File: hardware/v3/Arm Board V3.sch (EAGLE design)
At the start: 48 parts, among them CN1 1X4-BIG, IC1 L6208D, IC2 L6208D, IC3 L6208D, Q3 Q_LTC490, U1 MAX3468CSA

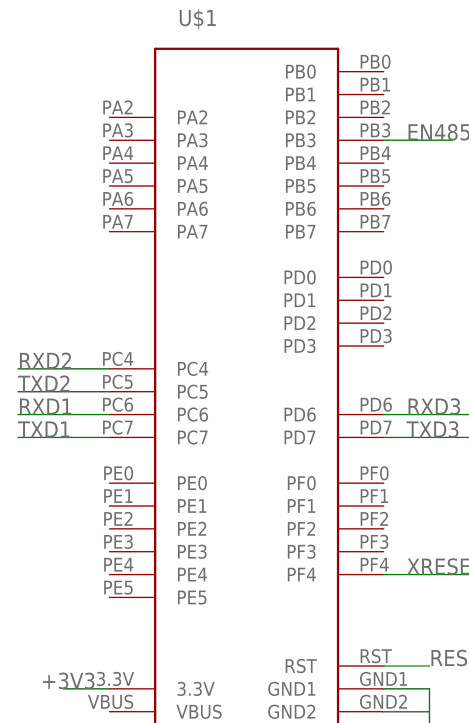
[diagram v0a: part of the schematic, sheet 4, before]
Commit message: Added enable pins to schematic and routed
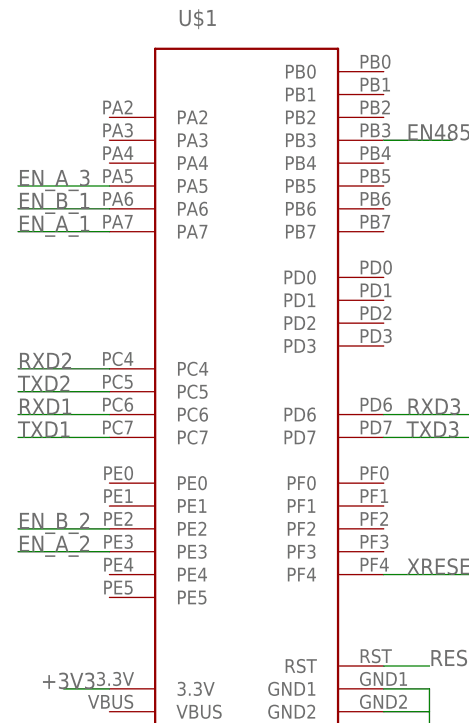
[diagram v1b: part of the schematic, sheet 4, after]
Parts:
- added H5: (no value), Lib_TH:H_MNTHOLE_#4
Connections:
- net EN_A_1: now also U$1.PA7
- net EN_A_2: now also U$1.PE3
- net EN_A_3: now also U$1.PA5
- net EN_B_1: now also U$1.PA6
- net EN_B_2: now also U$1.PE2
- net GND: now also H5.1
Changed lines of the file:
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@@
 <part name="GND13" library="SparkFun-Aesthetics" deviceset="GND" device=""/>
 <part name="GND14" library="SparkFun-Aesthetics" deviceset="GND" device=""/>
+<part name="H5" library="Lib_TH" deviceset="H_MNTHOLE" device="_#4"/>
+<part name="GND15" library="SparkFun-Aesthetics" deviceset="GND" device=""/>
 </parts>
 <sheets>
@@
 <instance part="GND13" gate="1" x="45.72" y="30.48"/>
 <instance part="GND14" gate="1" x="55.88" y="30.48"/>
+<instance part="H5" gate="G$1" x="66.04" y="38.1"/>
+<instance part="GND15" gate="1" x="66.04" y="30.48"/>
 </instances>
 <busses>
@@
 <pinref part="GND14" gate="1" pin="GND"/>
 <wire x1="55.88" y1="33.02" x2="55.88" y2="38.1" width="0.1524" layer="91"/>
+</segment>
+<segment>
+<pinref part="H5" gate="G$1" pin="1"/>
+<pinref part="GND15" gate="1" pin="GND"/>
+<wire x1="66.04" y1="33.02" x2="66.04" y2="38.1" width="0.1524" layer="91"/>
 </segment>
 </net>
@@
 </segment>
 </net>
+<net name="EN_A_1" class="0">
+<segment>
+<pinref part="U$1" gate="G$1" pin="PA7"/>
+<wire x1="12.7" y1="58.42" x2="2.54" y2="58.42" width="0.1524" layer="91"/>
+<label x="2.54" y="58.42" size="1.778" layer="95"/>
+</segment>
+</net>
+<net name="EN_A_3" class="0">
+<segment>
+<pinref part="U$1" gate="G$1" pin="PA5"/>
+<wire x1="12.7" y1="63.5" x2="2.54" y2="63.5" width="0.1524" layer="91"/>
+<label x="2.54" y="63.5" size="1.778" layer="95"/>
+</segment>
+</net>
+<net name="EN_A_2" class="0">
+<segment>
+<pinref part="U$1" gate="G$1" pin="PE3"/>
+<wire x1="12.7" y1="22.86" x2="2.54" y2="22.86" width="0.1524" layer="91"/>
+<label x="2.54" y="22.86" size="1.778" layer="95"/>
+</segment>
+</net>
+<net name="EN_B_2" class="0">
+<segment>
+<pinref part="U$1" gate="G$1" pin="PE2"/>
+<wire x1="12.7" y1="25.4" x2="2.54" y2="25.4" width="0.1524" layer="91"/>
+<label x="2.54" y="25.4" size="1.778" layer="95"/>
+</segment>
+</net>
+<net name="EN_B_1" class="0">
+<segment>
+<pinref part="U$1" gate="G$1" pin="PA6"/>
+<wire x1="12.7" y1="60.96" x2="2.54" y2="60.96" width="0.1524" layer="91"/>
+<label x="2.54" y="60.96" size="1.778" layer="95"/>
+</segment>
+</net>

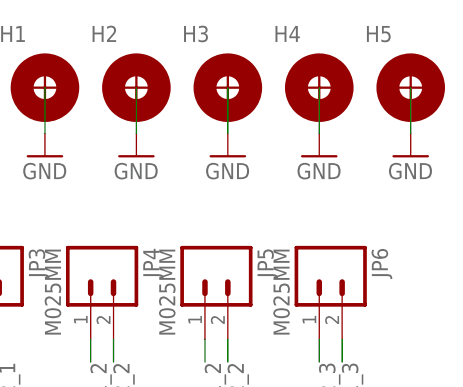
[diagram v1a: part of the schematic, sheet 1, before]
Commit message: Did some more routing on the board
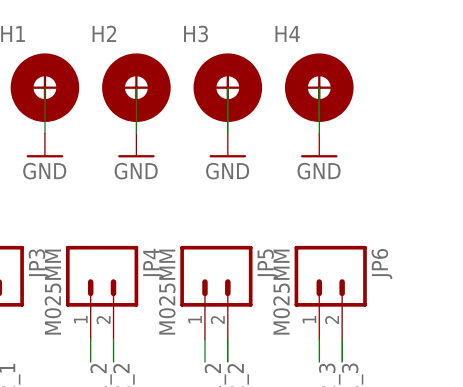
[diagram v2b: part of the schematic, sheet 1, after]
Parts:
- removed H5: (no value), Lib_TH:H_MNTHOLE_#4
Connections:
- removed net VS: C10.1, C3.1, C6.1, D2.A, D4.A, D6.A, IC1.VS_A, IC1.VS_B, IC2.VS_A, IC2.VS_B, IC3.VS_A, IC3.VS_B
- net GND: no longer H5.1
- net VIN: now also C10.1, C3.1, C6.1, D2.A, D4.A, D6.A, IC1.VS_A, IC1.VS_B, IC2.VS_A, IC2.VS_B, IC3.VS_A, IC3.VS_B

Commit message: Redid Xbee as well as moved things around
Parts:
- removed U$2: XBEE-1B2, SparkFun-RF:XBEE-1B2
- added C16: 0.1uF, SparkFun-Capacitors:0.1UF-25V(+80/-20%)(0603)
- added LED1, LED2: Red, SparkFun-LED:LED-RED0603
- added LED3, LED4, LED5: Green, SparkFun-LED:LED-GREEN0603
- added R12, R13, R14, R15, R16: 1k, SparkFun-Resistors:1KOHM1/10W1%(0603)
- added SJ2: SOLDERJUMPERTRACE, SparkFun:SOLDERJUMPERTRACE
- added U2: XBEE-1B3, SparkFun:XBEE-1B3
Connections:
- new net CTS: U2.CTS
- new net DIO0: U2.DIO0
- new net DIO1: U2.DIO1
- new net DIO11: U2.DIO11
- new net DIO12: U2.DIO12
- new net DIO2: U2.DIO2
- new net DIO3: SJ2.2, U2.DIO3
- new net DIO4: U2.DIO4
- new net DIO5: R16.2, U2.DIO5
- new net DIO9: U2.DIO9
- new net DTR: U2.DTR
- new net N$11: C16.2, SJ2.1
- new net N$139: LED5.A, R16.1
- new net N$38: LED1.A, R12.1
- new net N$4: LED2.A, R13.2
- new net N$6: LED3.A, R14.2
- new net N$7: LED4.A, R15.1
- new net RES1: U2.RES@8
- new net RES2: U2.RES@14
- new net RSSI: R15.2, U2.RSSI
- new net RTS: U2.RTS
- net +3V3: now also R12.2, R13.1, R14.1, U2.VDD; no longer U$2.VDD
- net GND: now also LED1.C, LED4.C, LED5.C, U2.GND; no longer U$2.GND
- net RXD3: now also LED2.C, U2.DOUT; no longer U$2.DOUT
- net TXD3: now also LED3.C, U2.DIN; no longer U$2.DIN
- net XRESET: now also C16.1, U2.RESET; no longer U$2.RESET

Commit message: Changed some stuff on launchpad
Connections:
- new net +5V: U$1.VBUS
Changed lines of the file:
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@@
 <part name="R15" library="SparkFun-Resistors" deviceset="1KOHM1/10W1%(0603)" device="" value="1k"/>
 <part name="GND17" library="SparkFun" deviceset="GND" device=""/>
-<part name="P+2" library="SparkFun" deviceset="3.3V" device=""/>
-<part name="P+3" library="SparkFun" deviceset="3.3V" device=""/>
-<part name="+3V3" library="SparkFun" deviceset="3.3V" device=""/>
 <part name="SJ2" library="SparkFun" deviceset="SOLDERJUMPER" device="TRACE"/>
 <part name="C16" library="SparkFun-Capacitors" deviceset="0.1UF-25V(+80/-20%)(0603)" device="" value="0.1uF"/>
@@
 </segment>
 </net>
+<net name="+5V" class="0">
+<segment>
+<pinref part="U$1" gate="G$1" pin="VBUS"/>
+<wire x1="12.7" y1="5.08" x2="7.62" y2="5.08" width="0.1524" layer="91"/>
+<label x="5.08" y="5.08" size="1.778" layer="95"/>
+</segment>
+</net>
 </nets>
 </sheet>
@@
 <instance part="R15" gate="G$1" x="17.78" y="81.28" rot="R90"/>
 <instance part="GND17" gate="1" x="17.78" y="60.96"/>
-<instance part="P+2" gate="G$1" x="30.48" y="88.9"/>
-<instance part="P+3" gate="G$1" x="5.08" y="88.9"/>
-<instance part="+3V3" gate="G$1" x="-5.08" y="88.9"/>
 <instance part="SJ2" gate="1" x="68.58" y="45.72"/>
 <instance part="C16" gate="G$1" x="50.8" y="45.72" rot="R90"/>
@@
 <wire x1="-5.08" y1="66.04" x2="-5.08" y2="63.5" width="0.1524" layer="91"/>
 <pinref part="LED2" gate="G$1" pin="C"/>
-<label x="-5.08" y="63.5" size="1.27" layer="95" rot="R270" xref="yes"/>
+<label x="-5.08" y="63.5" size="1.778" layer="95"/>
 </segment>
 <segment>
@@
 <wire x1="45.72" y1="86.36" x2="45.72" y2="88.9" width="0.1524" layer="91"/>
 <pinref part="R16" gate="G$1" pin="2"/>
-<label x="45.72" y="88.9" size="1.27" layer="95" rot="R90" xref="yes"/>
+<label x="45.72" y="88.9" size="1.778" layer="95"/>
 </segment>
 </net>
@@
 <wire x1="73.66" y1="45.72" x2="81.28" y2="45.72" width="0.1524" layer="91"/>
 <pinref part="SJ2" gate="1" pin="2"/>
-<label x="81.28" y="45.72" size="1.27" layer="95" xref="yes"/>
+<label x="81.28" y="45.72" size="1.778" layer="95"/>
 </segment>
 </net>
@@
 <wire x1="17.78" y1="86.36" x2="17.78" y2="88.9" width="0.1524" layer="91"/>
 <pinref part="R15" gate="G$1" pin="2"/>
-<label x="17.78" y="88.9" size="1.27" layer="95" rot="R90" xref="yes"/>
+<label x="17.78" y="88.9" size="1.778" layer="95"/>
 </segment>
 </net>
@@
 <wire x1="-5.08" y1="86.36" x2="-5.08" y2="88.9" width="0.1524" layer="91"/>
 <pinref part="R13" gate="G$1" pin="1"/>
-<pinref part="+3V3" gate="G$1" pin="3.3V"/>
+<label x="-5.08" y="88.9" size="1.778" layer="95"/>
 </segment>
 <segment>
 <wire x1="30.48" y1="88.9" x2="30.48" y2="86.36" width="0.1524" layer="91"/>
 <pinref part="R12" gate="G$1" pin="2"/>
-<pinref part="P+2" gate="G$1" pin="3.3V"/>
+<label x="30.48" y="88.9" size="1.778" layer="95"/>
 </segment>
 <segment>
 <wire x1="5.08" y1="86.36" x2="5.08" y2="88.9" width="0.1524" layer="91"/>
 <pinref part="R14" gate="G$1" pin="1"/>
-<pinref part="P+3" gate="G$1" pin="3.3V"/>
+<label x="5.08" y="88.9" size="1.778" layer="95"/>
 </segment>
 </net>
@@
 <wire x1="5.08" y1="66.04" x2="5.08" y2="63.5" width="0.1524" layer="91"/>
 <pinref part="LED3" gate="G$1" pin="C"/>
-<label x="5.08" y="63.5" size="1.27" layer="95" rot="R270" xref="yes"/>
+<label x="5.08" y="63.5" size="1.778" layer="95"/>
 </segment>
 </net>
@@
 <wire x1="45.72" y1="45.72" x2="35.56" y2="45.72" width="0.1524" layer="91"/>
 <pinref part="C16" gate="G$1" pin="1"/>
-<label x="35.56" y="45.72" size="1.27" layer="95" rot="R180" xref="yes"/>
-</segment>
-</net>
+<label x="35.56" y="45.72" size="1.778" layer="95"/>
+</segment>
+</net>

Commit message: Routed stuffs and stuffs and moved stuff and stuffs
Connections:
- net EN_A_1: now also U$1.PE1; no longer U$1.PA7
- net EN_A_2: now also U$1.PB7; no longer U$1.PE3
- net EN_A_3: no longer U$1.PA5
- net EN_B_1: now also U$1.PE2; no longer U$1.PA6
- net EN_B_2: now also U$1.PB6; no longer U$1.PE2
- net IN1_A_1: now also U$1.PD1
- net IN1_A_2: now also U$1.PA4
- net IN1_B_1: now also U$1.PD2
- net IN1_B_2: now also U$1.PA2
- net IN2_A_1: now also U$1.PD0
- net IN2_A_2: now also U$1.PA3
- net IN2_B_1: now also U$1.PD3
- net IN2_B_2: now also U$1.PE0
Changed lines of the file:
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@@
-</segment>
-</net>
-<net name="EN_A_1" class="0">
-<segment>
-<pinref part="U$1" gate="G$1" pin="PA7"/>
-<wire x1="12.7" y1="58.42" x2="2.54" y2="58.42" width="0.1524" layer="91"/>
-<label x="2.54" y="58.42" size="1.778" layer="95"/>
-</segment>
-</net>
-<net name="EN_A_3" class="0">
-<segment>
-<pinref part="U$1" gate="G$1" pin="PA5"/>
-<wire x1="12.7" y1="63.5" x2="2.54" y2="63.5" width="0.1524" layer="91"/>
-<label x="2.54" y="63.5" size="1.778" layer="95"/>
-</segment>
-</net>
-<net name="EN_A_2" class="0">
-<segment>
-<pinref part="U$1" gate="G$1" pin="PE3"/>
-<wire x1="12.7" y1="22.86" x2="2.54" y2="22.86" width="0.1524" layer="91"/>
-<label x="2.54" y="22.86" size="1.778" layer="95"/>
-</segment>
-</net>
-<net name="EN_B_2" class="0">
-<segment>
-<pinref part="U$1" gate="G$1" pin="PE2"/>
-<wire x1="12.7" y1="25.4" x2="2.54" y2="25.4" width="0.1524" layer="91"/>
-<label x="2.54" y="25.4" size="1.778" layer="95"/>
-</segment>
-</net>
-<net name="EN_B_1" class="0">
-<segment>
-<pinref part="U$1" gate="G$1" pin="PA6"/>
-<wire x1="12.7" y1="60.96" x2="2.54" y2="60.96" width="0.1524" layer="91"/>
-<label x="2.54" y="60.96" size="1.778" layer="95"/>
 </segment>
 </net>
@@
 </segment>
 </net>
+<net name="IN2_A_1" class="0">
+<segment>
+<pinref part="U$1" gate="G$1" pin="PD0"/>
+<wire x1="43.18" y1="53.34" x2="50.8" y2="53.34" width="0.1524" layer="91"/>
+<label x="45.72" y="53.34" size="1.778" layer="95"/>
+</segment>
+</net>
+<net name="IN1_B_1" class="0">
+<segment>
+<pinref part="U$1" gate="G$1" pin="PD2"/>
+<wire x1="43.18" y1="48.26" x2="50.8" y2="48.26" width="0.1524" layer="91"/>
+<label x="45.72" y="48.26" size="1.778" layer="95"/>
+</segment>
+</net>
+<net name="IN2_B_1" class="0">
+<segment>
+<pinref part="U$1" gate="G$1" pin="PD3"/>
+<wire x1="43.18" y1="45.72" x2="50.8" y2="45.72" width="0.1524" layer="91"/>
+<label x="45.72" y="45.72" size="1.778" layer="95"/>
+</segment>
+</net>
+<net name="EN_A_1" class="0">
+<segment>
+<pinref part="U$1" gate="G$1" pin="PE1"/>
+<wire x1="12.7" y1="27.94" x2="2.54" y2="27.94" width="0.1524" layer="91"/>
+<label x="2.54" y="27.94" size="1.778" layer="95"/>
+</segment>
+</net>
+<net name="EN_B_1" class="0">
+<segment>
+<pinref part="U$1" gate="G$1" pin="PE2"/>
+<wire x1="12.7" y1="25.4" x2="2.54" y2="25.4" width="0.1524" layer="91"/>
+<label x="2.54" y="25.4" size="1.778" layer="95"/>
+</segment>
+</net>
+<net name="IN1_A_1" class="0">
+<segment>
+<pinref part="U$1" gate="G$1" pin="PD1"/>
+<wire x1="43.18" y1="50.8" x2="50.8" y2="50.8" width="0.1524" layer="91"/>
+<label x="45.72" y="50.8" size="1.778" layer="95"/>
+</segment>
+</net>
+<net name="IN1_B_2" class="0">
+<segment>
+<pinref part="U$1" gate="G$1" pin="PA2"/>
+<wire x1="12.7" y1="71.12" x2="2.54" y2="71.12" width="0.1524" layer="91"/>
+<label x="2.54" y="71.12" size="1.778" layer="95"/>
+</segment>
+</net>
+<net name="IN2_A_2" class="0">
+<segment>
+<pinref part="U$1" gate="G$1" pin="PA3"/>
+<wire x1="12.7" y1="68.58" x2="2.54" y2="68.58" width="0.1524" layer="91"/>
+<label x="2.54" y="68.58" size="1.778" layer="95"/>
+</segment>
+</net>
+<net name="IN1_A_2" class="0">
+<segment>
+<pinref part="U$1" gate="G$1" pin="PA4"/>
+<wire x1="12.7" y1="66.04" x2="2.54" y2="66.04" width="0.1524" layer="91"/>
+<label x="2.54" y="66.04" size="1.778" layer="95"/>
+</segment>
+</net>
+<net name="EN_B_2" class="0">
+<segment>
+<pinref part="U$1" gate="G$1" pin="PB6"/>
+<wire x1="43.18" y1="60.96" x2="50.8" y2="60.96" width="0.1524" layer="91"/>
+<label x="45.72" y="60.96" size="1.778" layer="95"/>
+</segment>
+</net>
+<net name="EN_A_2" class="0">
+<segment>
+<pinref part="U$1" gate="G$1" pin="PB7"/>
+<wire x1="43.18" y1="58.42" x2="50.8" y2="58.42" width="0.1524" layer="91"/>
+<label x="45.72" y="58.42" size="1.778" layer="95"/>
+</segment>
+</net>
+<net name="IN2_B_2" class="0">
+<segment>
+<pinref part="U$1" gate="G$1" pin="PE0"/>
+<wire x1="12.7" y1="30.48" x2="2.54" y2="30.48" width="0.1524" layer="91"/>
+<label x="2.54" y="30.48" size="1.778" layer="95"/>
+</segment>
+</net>

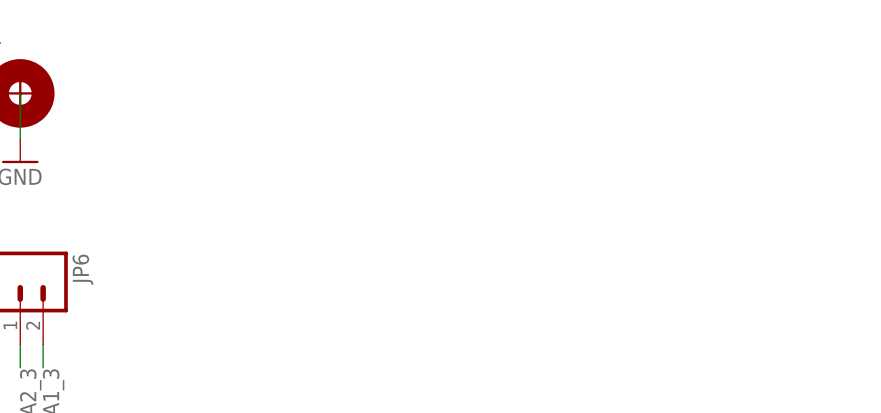
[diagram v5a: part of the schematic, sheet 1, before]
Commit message: Routing and Voltage Regulators (See Notes)
Started to route all of the pins towards the processor.  They need to be
reordered/reassigned since they do not make routing sense.  Added the
+12V and +18V regulators and hooked them up.  The +3V3 and +5V still
need to be picked and placed.
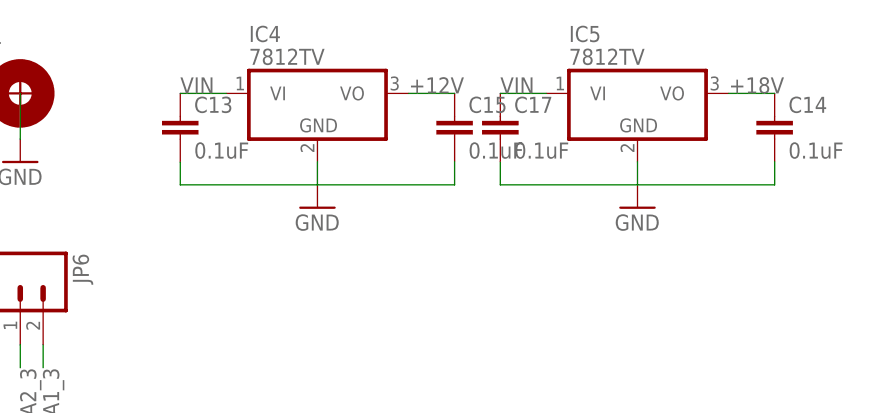
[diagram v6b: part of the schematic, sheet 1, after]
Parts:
- added C13, C14, C15, C17: 0.1uF, SparkFun-Capacitors:0.1UF-25V(+80/-20%)(0603)
- added IC4, IC5: 7812TV, linear:7812TV
- U1: value MAX3468CSA -> MAX3468CPA; device maxim:MAX3468CSA -> maxim:MAX3468CPA
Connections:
- new net +12V: C15.1, C3.1, D2.A, IC3.VS_A, IC3.VS_B, IC4.VO
- net +18V: now also C14.1, IC5.VO
- net EN_A_3: now also U$1.PB0
- net GND: now also C13.2, C14.2, C15.2, C17.2, IC4.GND, IC5.GND
- net IN1_A_3: now also U$1.PB1
- net IN2_A_3: now also U$1.PB2
- net VIN: now also C13.1, C17.1, IC4.VI, IC5.VI; no longer C3.1, D2.A, IC3.VS_A, IC3.VS_B
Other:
- note added: "TEMP!!! REPLACE!!!"
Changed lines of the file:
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@@
 <part name="IC2" library="L6206D" deviceset="L6208" device="D"/>
 <part name="IC3" library="L6206D" deviceset="L6208" device="D"/>
-<part name="U1" library="maxim" deviceset="MAX34*" device="SA" technology="68C" value="MAX3468CSA"/>
+<part name="U1" library="maxim" deviceset="MAX34*" device="PA" technology="68C" value="MAX3468CPA"/>
 <part name="CN1" library="adafruit" deviceset="1X4" device="-BIG"/>
 <part name="JP1" library="SparkFun-Connectors" deviceset="M02" device="5MM"/>
@@
 <part name="R16" library="SparkFun-Resistors" deviceset="1KOHM1/10W1%(0603)" device="" value="1k"/>
 <part name="GND31" library="SparkFun" deviceset="GND" device=""/>
+<part name="IC4" library="linear" deviceset="78*" device="TV" technology="12" value="7812TV"/>
+<part name="GND15" library="SparkFun-Aesthetics" deviceset="GND" device=""/>
+<part name="IC5" library="linear" deviceset="78*" device="TV" technology="12" value="7812TV"/>
+<part name="GND16" library="SparkFun-Aesthetics" deviceset="GND" device=""/>
+<part name="C13" library="SparkFun-Capacitors" deviceset="0.1UF-25V(+80/-20%)(0603)" device="" value="0.1uF"/>
+<part name="C14" library="SparkFun-Capacitors" deviceset="0.1UF-25V(+80/-20%)(0603)" device="" value="0.1uF"/>
+<part name="C15" library="SparkFun-Capacitors" deviceset="0.1UF-25V(+80/-20%)(0603)" device="" value="0.1uF"/>
+<part name="C17" library="SparkFun-Capacitors" deviceset="0.1UF-25V(+80/-20%)(0603)" device="" value="0.1uF"/>
 </parts>
 <sheets>
@@
 <instance part="GND13" gate="1" x="45.72" y="30.48"/>
 <instance part="GND14" gate="1" x="55.88" y="30.48"/>
+<instance part="IC4" gate="A1" x="88.9" y="38.1"/>
+<instance part="GND15" gate="1" x="88.9" y="25.4"/>
+<instance part="IC5" gate="A1" x="124.46" y="38.1"/>
+<instance part="GND16" gate="1" x="124.46" y="25.4"/>
+<instance part="C13" gate="G$1" x="73.66" y="33.02"/>
+<instance part="C14" gate="G$1" x="139.7" y="33.02"/>
+<instance part="C15" gate="G$1" x="104.14" y="33.02"/>
+<instance part="C17" gate="G$1" x="109.22" y="33.02"/>
 </instances>
 <busses>
@@
 <wire x1="55.88" y1="33.02" x2="55.88" y2="38.1" width="0.1524" layer="91"/>
 </segment>
+<segment>
+<pinref part="IC4" gate="A1" pin="GND"/>
+<wire x1="88.9" y1="30.48" x2="88.9" y2="27.94" width="0.1524" layer="91"/>
+<pinref part="GND15" gate="1" pin="GND"/>
+<wire x1="88.9" y1="27.94" x2="73.66" y2="27.94" width="0.1524" layer="91"/>
+<wire x1="73.66" y1="27.94" x2="73.66" y2="30.48" width="0.1524" layer="91"/>
+<wire x1="88.9" y1="27.94" x2="104.14" y2="27.94" width="0.1524" layer="91"/>
+<wire x1="104.14" y1="27.94" x2="104.14" y2="30.48" width="0.1524" layer="91"/>
+<pinref part="C13" gate="G$1" pin="2"/>
+<pinref part="C15" gate="G$1" pin="2"/>
+</segment>
+<segment>
+<pinref part="IC5" gate="A1" pin="GND"/>
+<wire x1="124.46" y1="30.48" x2="124.46" y2="27.94" width="0.1524" layer="91"/>
+<pinref part="GND16" gate="1" pin="GND"/>
+<wire x1="124.46" y1="27.94" x2="109.22" y2="27.94" width="0.1524" layer="91"/>
+<wire x1="109.22" y1="27.94" x2="109.22" y2="30.48" width="0.1524" layer="91"/>
+<wire x1="124.46" y1="27.94" x2="139.7" y2="27.94" width="0.1524" layer="91"/>
+<wire x1="139.7" y1="27.94" x2="139.7" y2="30.48" width="0.1524" layer="91"/>
+<pinref part="C14" gate="G$1" pin="2"/>
+<pinref part="C17" gate="G$1" pin="2"/>
+</segment>
 </net>
 <net name="A1_1" class="0">
@@
 <label x="5.08" y="27.94" size="1.778" layer="95" rot="R180"/>
 </segment>
+<segment>
+<pinref part="IC4" gate="A1" pin="VI"/>
+<wire x1="78.74" y1="38.1" x2="73.66" y2="38.1" width="0.1524" layer="91"/>
+<label x="73.66" y="38.1" size="1.778" layer="95"/>
+<pinref part="C13" gate="G$1" pin="1"/>
+</segment>
+<segment>
+<pinref part="IC5" gate="A1" pin="VI"/>
+<wire x1="114.3" y1="38.1" x2="109.22" y2="38.1" width="0.1524" layer="91"/>
+<label x="109.22" y="38.1" size="1.778" layer="95"/>
+<pinref part="C17" gate="G$1" pin="1"/>
+</segment>
 </net>
 <net name="A1_3" class="0">
@@
 <wire x1="58.42" y1="10.16" x2="58.42" y2="7.62" width="0.1524" layer="91"/>
 <label x="58.42" y="7.62" size="1.778" layer="95" rot="R270"/>
+</segment>
+</net>
+<net name="+12V" class="0">
+<segment>
+<pinref part="IC4" gate="A1" pin="VO"/>
+<wire x1="99.06" y1="38.1" x2="104.14" y2="38.1" width="0.1524" layer="91"/>
+<label x="99.06" y="38.1" size="1.778" layer="95"/>
+<pinref part="C15" gate="G$1" pin="1"/>
+</segment>
+</net>
+<net name="+18V" class="0">
+<segment>
+<pinref part="IC5" gate="A1" pin="VO"/>
+<wire x1="134.62" y1="38.1" x2="139.7" y2="38.1" width="0.1524" layer="91"/>
+<label x="134.62" y="38.1" size="1.778" layer="95"/>
+<pinref part="C14" gate="G$1" pin="1"/>
 </segment>
 </net>
@@
 <junction x="45.72" y="25.4"/>
 </segment>
+</net>
+<net name="+12V" class="0">
 <segment>
 <pinref part="C3" gate="G$1" pin="1"/>
@@
 <description>Processor</description>
 <plain>
+<text x="53.34" y="73.66" size="1.778" layer="91" align="center-left">TEMP!!!
+REPLACE!!!</text>
 </plain>
 <instances>
@@
 <wire x1="12.7" y1="30.48" x2="2.54" y2="30.48" width="0.1524" layer="91"/>
 <label x="2.54" y="30.48" size="1.778" layer="95"/>
+</segment>
+</net>
+<net name="EN_A_3" class="0">
+<segment>
+<pinref part="U$1" gate="G$1" pin="PB0"/>
+<wire x1="43.18" y1="76.2" x2="50.8" y2="76.2" width="0.1524" layer="91"/>
+</segment>
+</net>
+<net name="IN1_A_3" class="0">
+<segment>
+<pinref part="U$1" gate="G$1" pin="PB1"/>
+<wire x1="43.18" y1="73.66" x2="50.8" y2="73.66" width="0.1524" layer="91"/>
+</segment>
+</net>
+<net name="IN2_A_3" class="0">
+<segment>
+<pinref part="U$1" gate="G$1" pin="PB2"/>
+<wire x1="43.18" y1="71.12" x2="50.8" y2="71.12" width="0.1524" layer="91"/>
 </segment>
 </net>
@@
 </schematic>
 </drawing>
+<compatibility>
+<note version="6.3" minversion="6.2.2" severity="warning">
+Since Version 6.2.2 text objects can contain more than one line,
+which will not be processed correctly with this version.
+</note>
+</compatibility>
 </eagle>
